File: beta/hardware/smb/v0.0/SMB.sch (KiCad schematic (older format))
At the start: 1 part, among them IC101 ATMEGA168-P

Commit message: SPI, clock, I2C, Misc schematic upgrade
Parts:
- removed IC101: ATMEGA168-P, DIL28, symbol ATMEGA168-P
- added C101, C102: 0.1uF, SM0603, symbol C
- added C? (x2): 18pF, SM0603, symbol C
- added C? (x2): 0.1uF, symbol C
- added D?: LED, symbol LED
- added IC?: ATMEGA168-A, TQFP32, symbol ATMEGA168-A
- added J?: RTS_RESET, symbol 2PIN
- added J?: SERIAL_REV, symbol 6PIN
- added J?: I2C, symbol 4PIN
- added J?: 3X2PIN, symbol 3X2PIN
- added R?: 0, SM0603, symbol R
- added R? (x3): R, symbol R
- added R?: 10k, symbol R
- added R?: 10k, SM0603, symbol R
- added SW?: reset_sw, symbol SW_PUSH_SMALL
- added X?: 16MHz, symbol CRYSTAL
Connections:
- net labels added: +3.3V, /RESET, ETH_CS, ETH_INT, MAIN_CLK, RX, SCL, SDA, SPI_CLK, SPI_MISO, SPI_MOSI, TX
- wire segments 3 -> 68
- no-connect marks 0 -> 1
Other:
- note added: "Not Mounted"
- note added: "Remove this to use Xtal"

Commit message: Some work on the SMD version of the SMB
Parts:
- removed IC?: ATMEGA168-A, TQFP32, symbol ATMEGA168-A
- removed J?: 3X2PIN, symbol 3X2PIN
- removed R?: 0, SM0603, symbol R
- added C103: 0.1uF, symbol C
- added IC101: ATMEGA1284-A, TQPF44, symbol ATMEGA1284-A
- added J?: ICSP, symbol 3X2PIN
- R102: renamed from R?; value R -> 3.3kR
- gave numbers to parts that had none: 14
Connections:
- net labels added: +5V, SPI_SCK
- net labels removed: +3.3V, MAIN_CLK
- wire segments 68 -> 79
- no-connect marks 1 -> 0
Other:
- note added: "ICSP Connector"
- note removed: "Remove this to use Xtal"
- moved on the sheet: C101, C102, C104, C105, C106, D101, R101, R102, X101

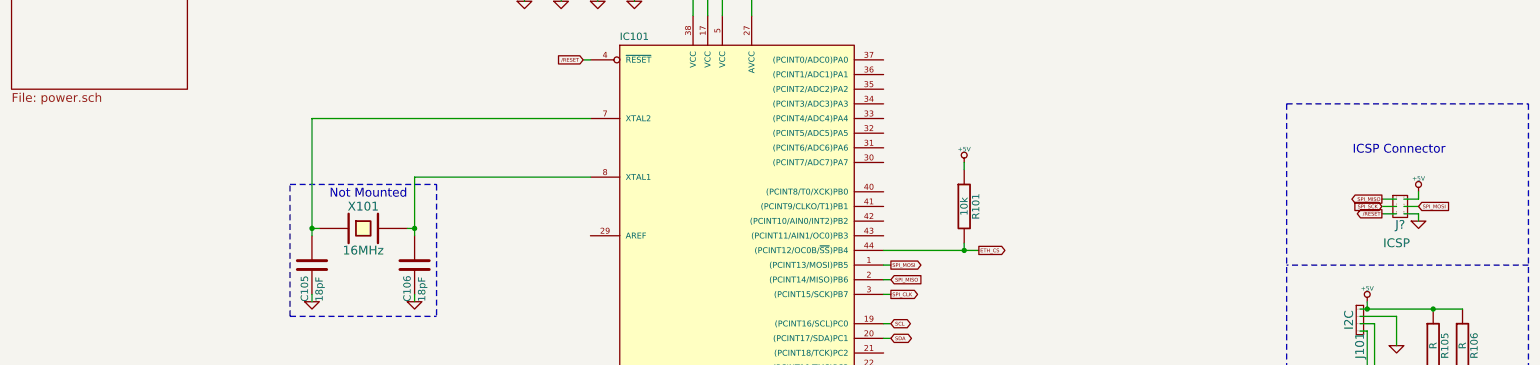
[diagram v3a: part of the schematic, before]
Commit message: Added uSD-Card and buffer schematic
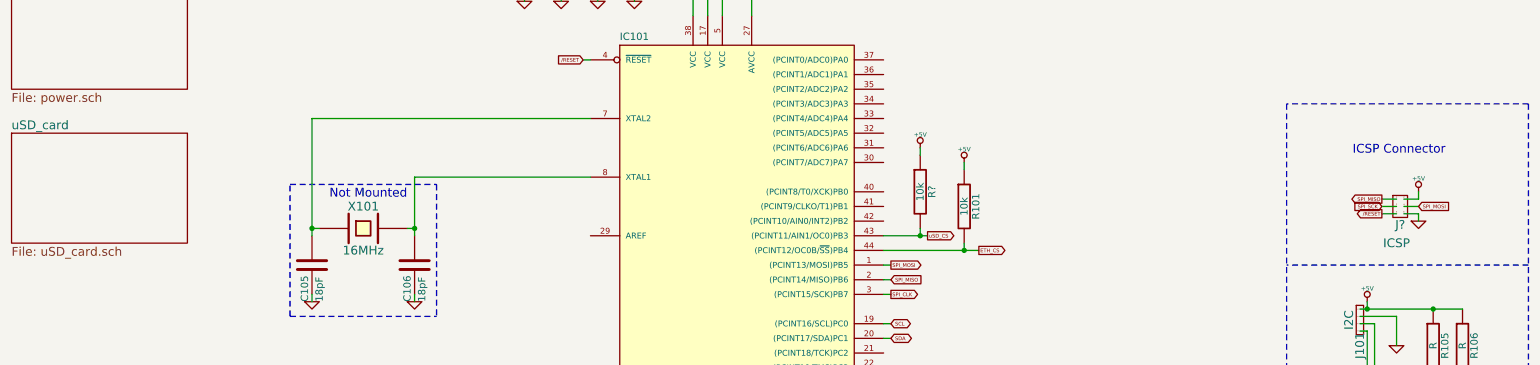
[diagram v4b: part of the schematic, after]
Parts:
- added R?: 10k, symbol R
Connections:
- net +5V: now also R?.1
- net uSD_CS: now reaches IC101.43 ((PCINT11/AIN1/OC0)PB3)
- net uSD_CS: now also R?.2
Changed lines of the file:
@@
-EESchema Schematic File Version 2  date 28/06/2012 23:43:20
+EESchema Schematic File Version 2  date 01/07/2012 20:02:11
 LIBS:power
 LIBS:device
@@
 LIBS:lm1117imp-3
 LIBS:mp2562ds
+LIBS:usd_conn
+LIBS:74lvc1g126gw
 LIBS:SMB-cache
 EELAYER 25  0
@@
 $Descr A4 11700 8267
 encoding utf-8
-Sheet 1 3
+Sheet 1 4
 Title ""
-Date "28 jun 2012"
+Date "1 jul 2012"
 Rev ""
 Comp ""
@@
 Comment4 ""
 $EndDescr
+Wire Wire Line
+	6800 2700 6800 2750
+Wire Wire Line
+	6850 3300 6550 3300
 Wire Notes Line
 	10950 2400 10950 6150
 Wire Notes Line
-	9300 2400 10950 2400
+	10950 2400 9300 2400
 Wire Notes Line
 	9300 2400 9300 6150
@@
 Wire Wire Line
 	9950 3050 10050 3050
+Wire Wire Line
+	6800 3250 6800 3300
+Connection ~ 6800 3300
+$Comp
+L +5V #PWR?
+U 1 1 4FF09080
+P 6800 2700
+F 0 "#PWR?" H 6800 2790 20  0001 C CNN
+F 1 "+5V" H 6800 2790 30  0000 C CNN
+	1    6800 2700
+	1    0    0    -1
+$EndComp
+$Comp
+L R R?
+U 1 1 4FF09065
+P 6800 3000
+F 0 "R?" V 6880 3000 50  0000 C CNN
+F 1 "10k" V 6800 3000 50  0000 C CNN
+	1    6800 3000
+	1    0    0    -1
+$EndComp
+Text GLabel 6850 3300 2    25   Output ~ 0
+uSD_CS
+$Sheet
+S 600  2600 1200 750
+U 4FF04C39
+F0 "uSD_card" 60
+F1 "uSD_card.sch" 60
+$EndSheet
 Text Notes 9750 2750 0    60   ~ 0
 ICSP Connector

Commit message: few modifications
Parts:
- gave numbers to parts that had none: 2
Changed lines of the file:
@@
-EESchema Schematic File Version 2  date 01/07/2012 20:02:11
+EESchema Schematic File Version 2  date 01/07/2012 23:30:37
 LIBS:power
 LIBS:device
@@
 Connection ~ 6800 3300
 $Comp
-L +5V #PWR?
+L +5V #PWR112
 U 1 1 4FF09080
 P 6800 2700
-F 0 "#PWR?" H 6800 2790 20  0001 C CNN
+F 0 "#PWR112" H 6800 2790 20  0001 C CNN
 F 1 "+5V" H 6800 2790 30  0000 C CNN
 	1    6800 2700
@@
 $EndComp
 $Comp
-L R R?
+L R R103
 U 1 1 4FF09065
 P 6800 3000
-F 0 "R?" V 6880 3000 50  0000 C CNN
+F 0 "R103" V 6880 3000 50  0000 C CNN
 F 1 "10k" V 6800 3000 50  0000 C CNN
 	1    6800 3000
@@
 SPI_MOSI
 $Comp
-L +5V #PWR?
+L +5V #PWR119
 U 1 1 4FDE4559
 P 10200 3000
-F 0 "#PWR?" H 10200 3090 20  0001 C CNN
+F 0 "#PWR119" H 10200 3090 20  0001 C CNN
 F 1 "+5V" H 10200 3090 30  0000 C CNN
 	1    10200 3000
@@
 $EndComp
 $Comp
-L GND #PWR?
+L GND #PWR120
 U 1 1 4FDE454D
 P 10200 3200
-F 0 "#PWR?" H 10200 3200 30  0001 C CNN
+F 0 "#PWR120" H 10200 3200 30  0001 C CNN
 F 1 "GND" H 10200 3130 30  0001 C CNN
 	1    10200 3200
@@
 $EndComp
 $Comp
-L 3X2PIN J?
+L 3X2PIN J103
 U 1 1 4FDE451A
 P 10050 3100
-F 0 "J?" H 10075 2975 60  0000 C CNN
+F 0 "J103" H 10075 2975 60  0000 C CNN
 F 1 "ICSP" H 10050 2850 60  0000 C CNN
 	1    10050 3100
@@
 $EndSheet
 $Comp
-L +5V #PWR115
+L +5V #PWR116
 U 1 1 4FDE1B12
 P 9850 3750
-F 0 "#PWR115" H 9850 3840 20  0001 C CNN
+F 0 "#PWR116" H 9850 3840 20  0001 C CNN
 F 1 "+5V" H 9850 3840 30  0000 C CNN
 	1    9850 3750
@@
 $EndComp
 $Comp
-L +5V #PWR114
+L +5V #PWR115
 U 1 1 4FDE1B05
 P 9650 5050
-F 0 "#PWR114" H 9650 5140 20  0001 C CNN
+F 0 "#PWR115" H 9650 5140 20  0001 C CNN
 F 1 "+5V" H 9650 5140 30  0000 C CNN
 	1    9650 5050
@@
 $EndComp
 $Comp
-L +5V #PWR119
+L +5V #PWR122
 U 1 1 4FDE1B01
 P 10850 5150
-F 0 "#PWR119" H 10850 5240 20  0001 C CNN
+F 0 "#PWR122" H 10850 5240 20  0001 C CNN
 F 1 "+5V" H 10850 5240 30  0000 C CNN
 	1    10850 5150
@@
 $EndComp
 $Comp
-L +5V #PWR112
+L +5V #PWR113
 U 1 1 4FDE1AEF
 P 7100 2800
-F 0 "#PWR112" H 7100 2890 20  0001 C CNN
+F 0 "#PWR113" H 7100 2890 20  0001 C CNN
 F 1 "+5V" H 7100 2890 30  0000 C CNN
 	1    7100 2800
@@
 SDA
 $Comp
-L GND #PWR117
+L GND #PWR118
 U 1 1 4FA06DB4
 P 10050 4050
-F 0 "#PWR117" H 10050 4050 30  0001 C CNN
+F 0 "#PWR118" H 10050 4050 30  0001 C CNN
 F 1 "GND" H 10050 3980 30  0001 C CNN
 	1    10050 4050
@@
 TX
 $Comp
-L GND #PWR118
+L GND #PWR121
 U 1 1 4FA025EE
 P 10600 5150
-F 0 "#PWR118" H 10600 5150 30  0001 C CNN
+F 0 "#PWR121" H 10600 5150 30  0001 C CNN
 F 1 "GND" H 10600 5080 30  0001 C CNN
 	1    10600 5150
@@
 /RESET
 $Comp
-L GND #PWR116
+L GND #PWR117
 U 1 1 4FA01B14
 P 9850 6050
-F 0 "#PWR116" H 9850 6050 30  0001 C CNN
+F 0 "#PWR117" H 9850 6050 30  0001 C CNN
 F 1 "GND" H 9850 5980 30  0001 C CNN
 	1    9850 6050
@@
 /RESET
 $Comp
-L GND #PWR113
+L GND #PWR114
 U 1 1 4FA01A42
 P 7750 5800
-F 0 "#PWR113" H 7750 5800 30  0001 C CNN
+F 0 "#PWR114" H 7750 5800 30  0001 C CNN
 F 1 "GND" H 7750 5730 30  0001 C CNN
 	1    7750 5800

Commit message: New components and corrections
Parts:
- C103, C104, C107, R102, R103, R104, R105, R106: footprint (none) -> SM0603
- D101: footprint (none) -> LED-0603
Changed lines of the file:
@@
-EESchema Schematic File Version 2  date 01/07/2012 23:30:37
+EESchema Schematic File Version 2  date 14/07/2012 20:45:27
 LIBS:power
 LIBS:device
@@
 LIBS:usd_conn
 LIBS:74lvc1g126gw
+LIBS:dual_self
 LIBS:SMB-cache
 EELAYER 25  0
@@
 Sheet 1 4
 Title ""
-Date "1 jul 2012"
+Date "14 jul 2012"
 Rev ""
 Comp ""
@@
 Connection ~ 6800 3300
 $Comp
-L +5V #PWR112
+L +5V #PWR01
 U 1 1 4FF09080
 P 6800 2700
-F 0 "#PWR112" H 6800 2790 20  0001 C CNN
+F 0 "#PWR01" H 6800 2790 20  0001 C CNN
 F 1 "+5V" H 6800 2790 30  0000 C CNN
 	1    6800 2700
@@
 F 0 "R103" V 6880 3000 50  0000 C CNN
 F 1 "10k" V 6800 3000 50  0000 C CNN
+F 2 "SM0603" V 6900 3000 50  0000 C CNN
 	1    6800 3000
 	1    0    0    -1
@@
 SPI_MOSI
 $Comp
-L +5V #PWR119
+L +5V #PWR02
 U 1 1 4FDE4559
 P 10200 3000
-F 0 "#PWR119" H 10200 3090 20  0001 C CNN
+F 0 "#PWR02" H 10200 3090 20  0001 C CNN
 F 1 "+5V" H 10200 3090 30  0000 C CNN
 	1    10200 3000
@@
 $EndComp
 $Comp
-L GND #PWR120
+L GND #PWR03
 U 1 1 4FDE454D
 P 10200 3200
-F 0 "#PWR120" H 10200 3200 30  0001 C CNN
+F 0 "#PWR03" H 10200 3200 30  0001 C CNN
 F 1 "GND" H 10200 3130 30  0001 C CNN
 	1    10200 3200
@@
 $EndSheet
 $Comp
-L +5V #PWR116
+L +5V #PWR04
 U 1 1 4FDE1B12
 P 9850 3750
-F 0 "#PWR116" H 9850 3840 20  0001 C CNN
+F 0 "#PWR04" H 9850 3840 20  0001 C CNN
 F 1 "+5V" H 9850 3840 30  0000 C CNN
 	1    9850 3750
@@
 $EndComp
 $Comp
-L +5V #PWR115
+L +5V #PWR05
 U 1 1 4FDE1B05
 P 9650 5050
-F 0 "#PWR115" H 9650 5140 20  0001 C CNN
+F 0 "#PWR05" H 9650 5140 20  0001 C CNN
 F 1 "+5V" H 9650 5140 30  0000 C CNN
 	1    9650 5050
@@
 $EndComp
 $Comp
-L +5V #PWR122
+L +5V #PWR06
 U 1 1 4FDE1B01
 P 10850 5150
-F 0 "#PWR122" H 10850 5240 20  0001 C CNN
+F 0 "#PWR06" H 10850 5240 20  0001 C CNN
 F 1 "+5V" H 10850 5240 30  0000 C CNN
 	1    10850 5150
@@
 $EndComp
 $Comp
-L +5V #PWR113
+L +5V #PWR07
 U 1 1 4FDE1AEF
 P 7100 2800
-F 0 "#PWR113" H 7100 2890 20  0001 C CNN
+F 0 "#PWR07" H 7100 2890 20  0001 C CNN
 F 1 "+5V" H 7100 2890 30  0000 C CNN
 	1    7100 2800
@@
 $EndComp
 $Comp
-L +5V #PWR108
+L +5V #PWR08
 U 1 1 4FDE1AE0
 P 5350 1000
-F 0 "#PWR108" H 5350 1090 20  0001 C CNN
+F 0 "#PWR08" H 5350 1090 20  0001 C CNN
 F 1 "+5V" H 5350 1090 30  0000 C CNN
 	1    5350 1000
@@
 $EndComp
 $Comp
-L GND #PWR109
+L GND #PWR09
 U 1 1 4FDE0BAB
 P 5350 5900
-F 0 "#PWR109" H 5350 5900 30  0001 C CNN
+F 0 "#PWR09" H 5350 5900 30  0001 C CNN
 F 1 "GND" H 5350 5830 30  0001 C CNN
 	1    5350 5900
@@
 $EndComp
 $Comp
-L GND #PWR107
+L GND #PWR010
 U 1 1 4FDE0BA8
 P 5250 5900
-F 0 "#PWR107" H 5250 5900 30  0001 C CNN
+F 0 "#PWR010" H 5250 5900 30  0001 C CNN
 F 1 "GND" H 5250 5830 30  0001 C CNN
 	1    5250 5900
@@
 $EndComp
 $Comp
-L GND #PWR110
+L GND #PWR011
 U 1 1 4FDE0BA5
 P 5450 5900
-F 0 "#PWR110" H 5450 5900 30  0001 C CNN
+F 0 "#PWR011" H 5450 5900 30  0001 C CNN
 F 1 "GND" H 5450 5830 30  0001 C CNN
 	1    5450 5900
@@
 $EndComp
 $Comp
-L GND #PWR111
+L GND #PWR012
 U 1 1 4FDE0BA2
 P 5550 5900
-F 0 "#PWR111" H 5550 5900 30  0001 C CNN
+F 0 "#PWR012" H 5550 5900 30  0001 C CNN
 F 1 "GND" H 5550 5830 30  0001 C CNN
 	1    5550 5900
@@
 $EndComp
 $Comp
-L GND #PWR106
+L GND #PWR013
 U 1 1 4FDE09A7
 P 4850 1700
-F 0 "#PWR106" H 4850 1700 30  0001 C CNN
+F 0 "#PWR013" H 4850 1700 30  0001 C CNN
 F 1 "GND" H 4850 1630 30  0001 C CNN
 	1    4850 1700
@@
 $EndComp
 $Comp
-L GND #PWR105
+L GND #PWR014
 U 1 1 4FDE09A4
 P 4600 1700
-F 0 "#PWR105" H 4600 1700 30  0001 C CNN
+F 0 "#PWR014" H 4600 1700 30  0001 C CNN
 F 1 "GND" H 4600 1630 30  0001 C CNN
 	1    4600 1700
@@
 $EndComp
 $Comp
-L GND #PWR104
+L GND #PWR015
 U 1 1 4FDE09A1
 P 4350 1700
-F 0 "#PWR104" H 4350 1700 30  0001 C CNN
+F 0 "#PWR015" H 4350 1700 30  0001 C CNN
 F 1 "GND" H 4350 1630 30  0001 C CNN
 	1    4350 1700
@@
 $EndComp
 $Comp
-L GND #PWR103
+L GND #PWR016
 U 1 1 4FDE099C
 P 4100 1700
-F 0 "#PWR103" H 4100 1700 30  0001 C CNN
+F 0 "#PWR016" H 4100 1700 30  0001 C CNN
 F 1 "GND" H 4100 1630 30  0001 C CNN
 	1    4100 1700
@@
 F 0 "C103" V 4150 1100 50  0000 L CNN
 F 1 "0.1uF" V 4050 1100 50  0000 L CNN
+F 2 "SM0603" V 4150 1100 50  0000 C CNN
 	1    4100 1350
 	1    0    0    -1
@@
 F 0 "IC101" H 4750 5630 50  0000 L BNN
 F 1 "ATMEGA1284-A" H 5750 1900 50  0000 L BNN
-F 2 "TQPF44" H 4900 1950 50  0001 C CNN
+F 2 "TQPF44" H 4900 1950 50  0000 C CNN
 	1    5550 3800
 	1    0    0    -1
@@
 SDA
 $Comp
-L GND #PWR118
+L GND #PWR017
 U 1 1 4FA06DB4
 P 10050 4050
-F 0 "#PWR118" H 10050 4050 30  0001 C CNN
+F 0 "#PWR017" H 10050 4050 30  0001 C CNN
 F 1 "GND" H 10050 3980 30  0001 C CNN
 	1    10050 4050
@@
 F 0 "R106" V 10580 4050 50  0000 C CNN
 F 1 "R" V 10500 4050 50  0000 C CNN
+F 2 "SM0603" V 10600 4050 50  0000 C CNN
 	1    10500 4050
 	1    0    0    -1
@@
 F 0 "R105" V 10380 4050 50  0000 C CNN
 F 1 "R" V 10300 4050 50  0000 C CNN
+F 2 "SM0603" V 10400 4050 50  0000 C CNN
 	1    10300 4050
 	1    0    0    -1
@@
 F 0 "R101" V 7180 3100 50  0000 C CNN
 F 1 "10k" V 7100 3100 50  0000 C CNN
-F 2 "SM0603" H 7100 3100 60  0001 C CNN
+F 2 "SM0603" H 7100 3100 60  0000 C CNN
 	1    7100 3100
 	1    0    0    -1
@@
 TX
 $Comp
-L GND #PWR121
+L GND #PWR018
 U 1 1 4FA025EE
 P 10600 5150
-F 0 "#PWR121" H 10600 5150 30  0001 C CNN
+F 0 "#PWR018" H 10600 5150 30  0001 C CNN
 F 1 "GND" H 10600 5080 30  0001 C CNN
 	1    10600 5150
@@
 F 0 "C107" H 10000 5500 50  0000 L CNN
 F 1 "0.1uF" H 10000 5300 50  0000 L CNN
+F 2 "SM0603" H 10000 5400 50  0000 C CNN
 	1    9950 5400
 	1    0    0    -1
@@
 /RESET
 $Comp
-L GND #PWR117
+L GND #PWR019
 U 1 1 4FA01B14
 P 9850 6050
-F 0 "#PWR117" H 9850 6050 30  0001 C CNN
+F 0 "#PWR019" H 9850 6050 30  0001 C CNN
 F 1 "GND" H 9850 5980 30  0001 C CNN
 	1    9850 6050
@@
 F 0 "R104" V 9730 5400 50  0000 C CNN
 F 1 "10k" V 9650 5400 50  0000 C CNN
+F 2 "SM0603" V 9750 5400 50  0000 C CNN
 	1    9650 5400
 	1    0    0    -1
@@
 /RESET
 $Comp
-L GND #PWR114
+L GND #PWR020
 U 1 1 4FA01A42
 P 7750 5800
-F 0 "#PWR114" H 7750 5800 30  0001 C CNN
+F 0 "#PWR020" H 7750 5800 30  0001 C CNN
 F 1 "GND" H 7750 5730 30  0001 C CNN
 	1    7750 5800
@@
 F 0 "R102" V 7830 5500 50  0000 C CNN
 F 1 "3.3kR" V 7750 5500 50  0000 C CNN
+F 2 "SM0603" V 7850 5500 50  0000 C CNN
 	1    7750 5500
 	1    0    0    -1
@@
 F 0 "D101" H 7500 5300 50  0000 C CNN
 F 1 "LED" H 7500 5100 50  0000 C CNN
+F 2 "LED-0603" H 7500 5200 50  0000 C CNN
 	1    7500 5200
 	1    0    0    -1
@@
 F 0 "C104" V 4300 1400 50  0000 L CNN
 F 1 "0.1uF" V 4400 1400 50  0000 L CNN
+F 2 "SM0603" V 4500 1400 50  0000 C CNN
 	1    4350 1350
 	-1   0    0    1
 $EndComp
 $Comp
-L GND #PWR102
+L GND #PWR021
 U 1 1 4FA01409
 P 3350 3750
-F 0 "#PWR102" H 3350 3750 30  0001 C CNN
+F 0 "#PWR021" H 3350 3750 30  0001 C CNN
 F 1 "GND" H 3350 3680 30  0001 C CNN
 	1    3350 3750
@@
 $EndComp
 $Comp
-L GND #PWR101
+L GND #PWR022
 U 1 1 4FA01406
 P 2650 3750
-F 0 "#PWR101" H 2650 3750 30  0001 C CNN
+F 0 "#PWR022" H 2650 3750 30  0001 C CNN
 F 1 "GND" H 2650 3680 30  0001 C CNN
 	1    2650 3750
@@
 F 0 "C106" V 3300 3250 50  0000 L CNN
 F 1 "18pF" V 3400 3250 50  0000 L CNN
-F 2 "SM0603" H 3350 3500 60  0001 C CNN
+F 2 "SM0603" H 3350 3500 60  0000 C CNN
 	1    3350 3500
 	1    0    0    -1
@@
 F 0 "C105" V 2600 3250 50  0000 L CNN
 F 1 "18pF" V 2700 3250 50  0000 L CNN
-F 2 "SM0603" H 2650 3500 60  0001 C CNN
+F 2 "SM0603" H 2650 3500 60  0000 C CNN
 	1    2650 3500
 	1    0    0    -1
@@
 F 0 "C102" V 4900 1100 50  0000 L CNN
 F 1 "0.1uF" V 4800 1100 50  0000 L CNN
-F 2 "SM0603" H 4850 1350 60  0001 C CNN
+F 2 "SM0603" H 4850 1350 60  0000 C CNN
 	1    4850 1350
 	1    0    0    -1
@@
 F 0 "C101" V 4650 1100 50  0000 L CNN
 F 1 "0.1uF" V 4550 1100 50  0000 L CNN
-F 2 "SM0603" H 4600 1350 60  0001 C CNN
+F 2 "SM0603" H 4600 1350 60  0000 C CNN
 	1    4600 1350
 	1    0    0    -1
